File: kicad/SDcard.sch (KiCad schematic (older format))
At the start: 5 parts, among them J7 SD_Card, U25 74LVC244A

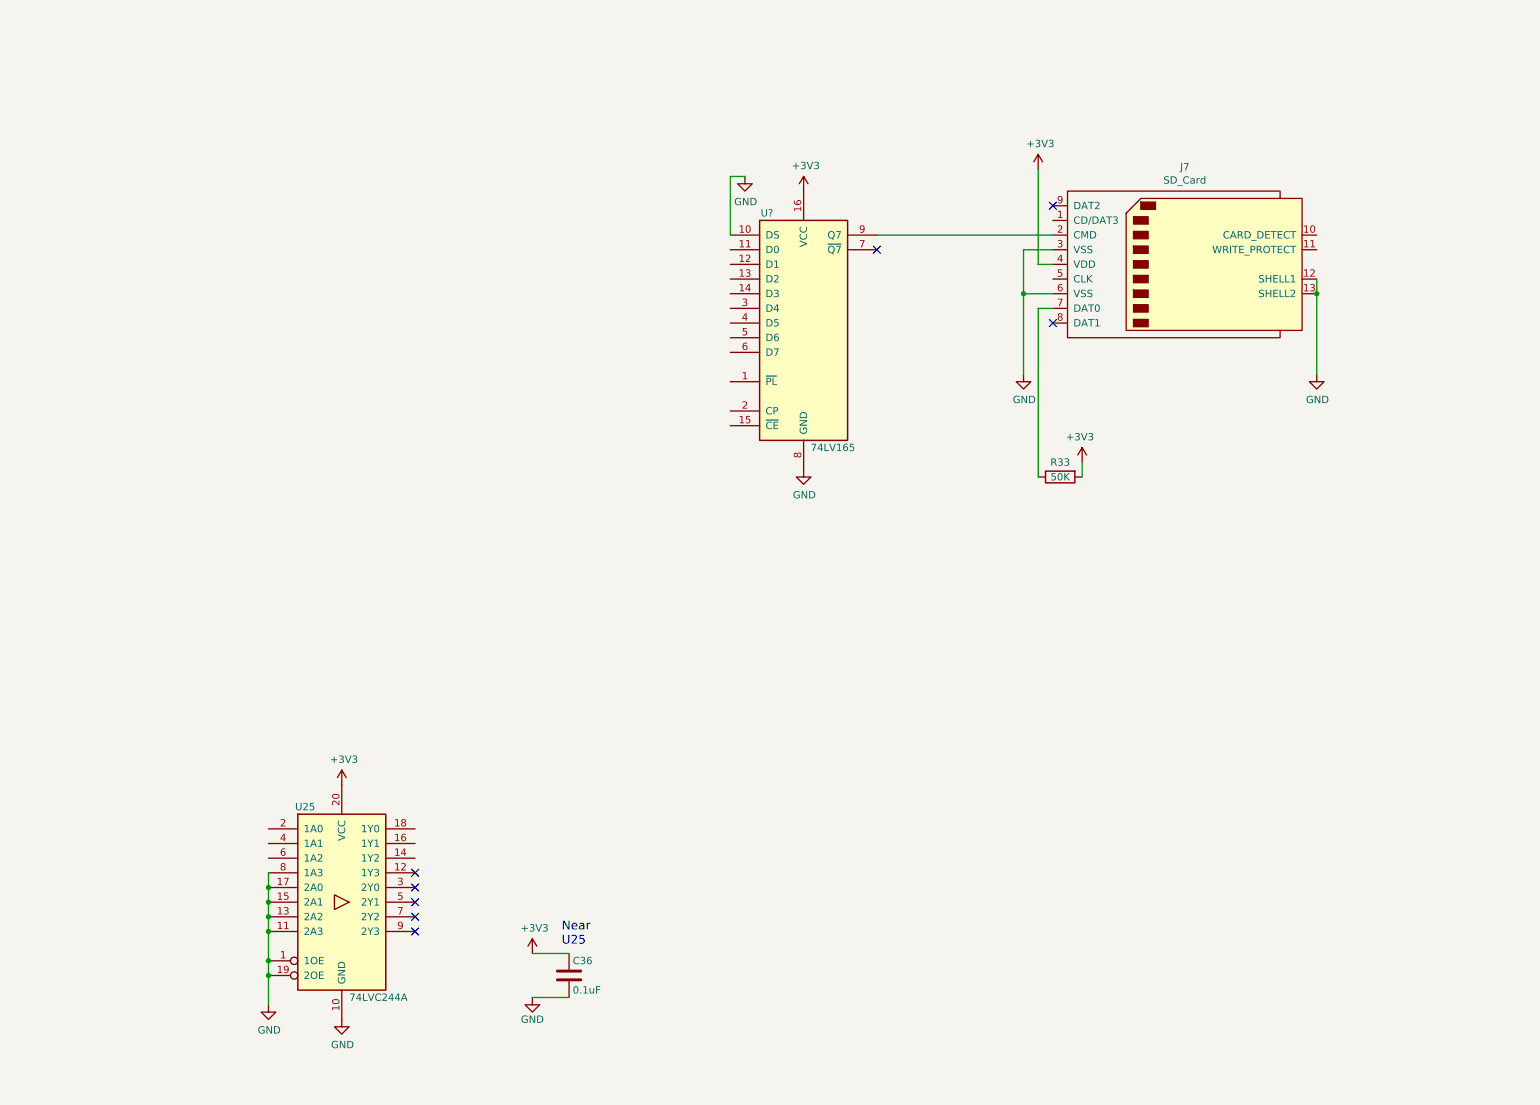
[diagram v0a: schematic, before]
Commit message: SDcard interface mostly complete.
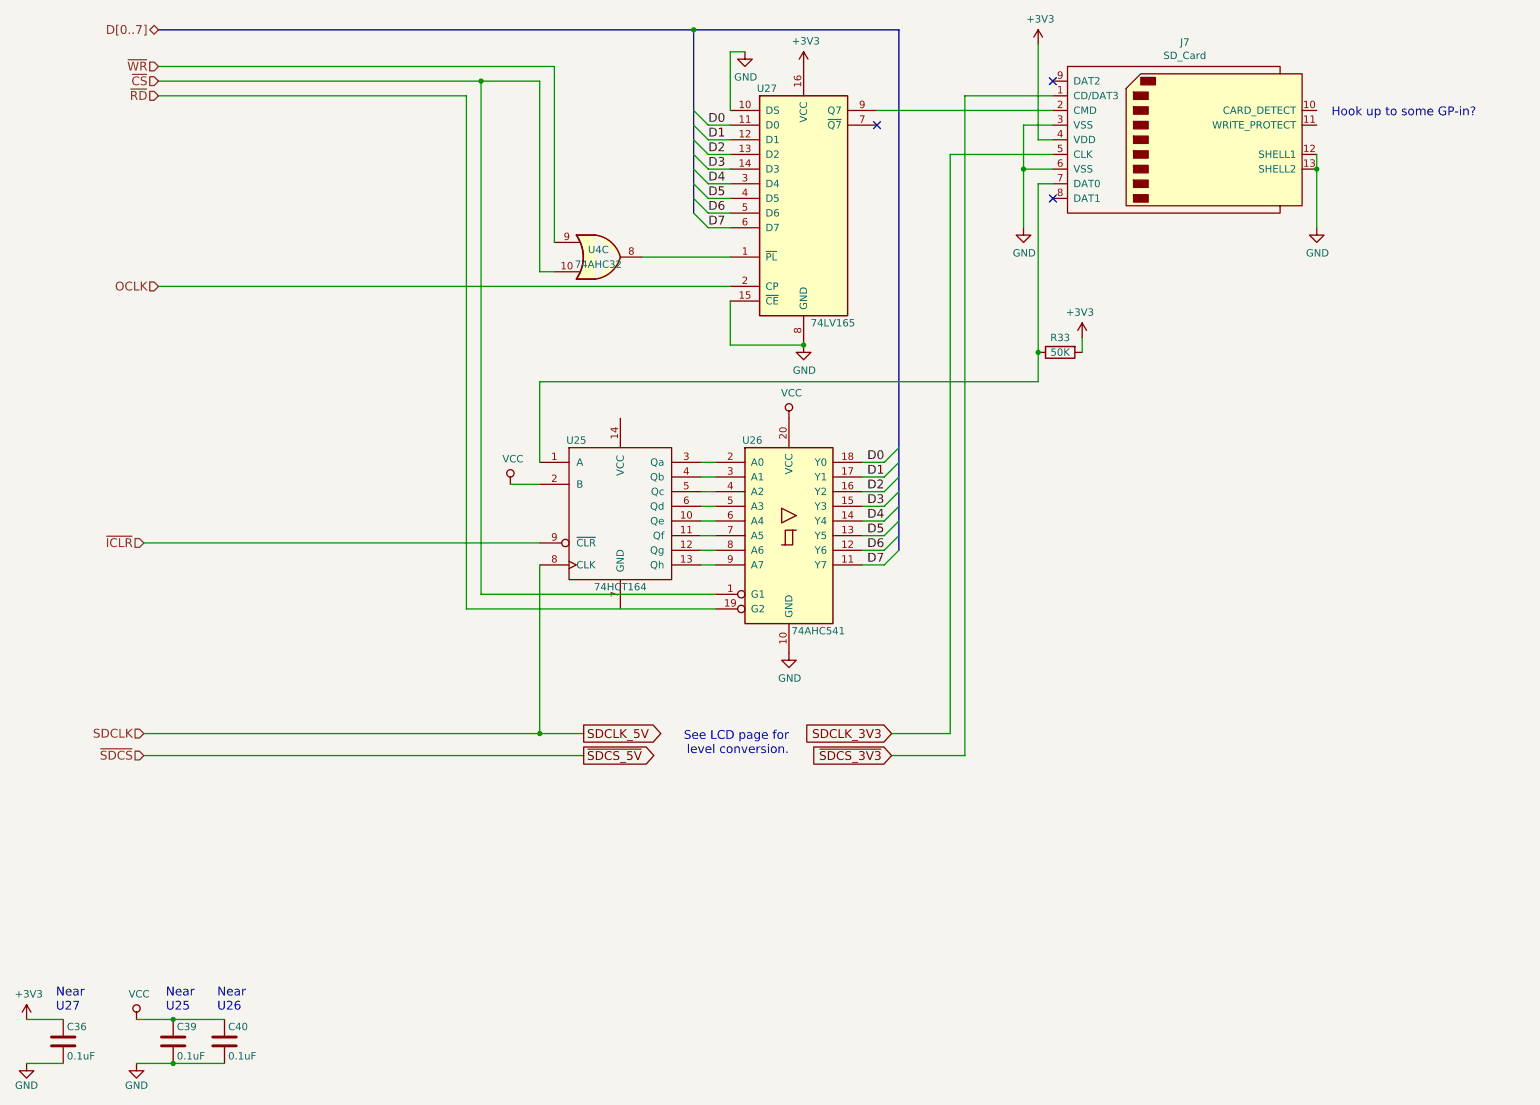
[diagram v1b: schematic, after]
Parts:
- removed U25: 74LVC244A, symbol 74xx:74HC244
- added C39, C40: 0.1uF, Capacitors_THT:C_Disc_D4.3mm_W1.9mm_P5.00mm, symbol Device:C
- added U25: 74HCT164, symbol headquarters:74HC164
- added U26: 74AHC541, symbol 74xx:74LS541
- added U4: 74AHC32, Housings_DIP:DIP-14_W7.62mm_LongPads, symbol 74xx:74LS32
- gave numbers to parts that had none: 1
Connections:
- net GND: now also U27.15 (~CE), C39.2, C40.2, U26.10 (GND)
- net at J7.7 (DAT0), R33.1: now also U25.1 (A)
- net at U27.1 (~PL): now also U4.8
- net D0: now reaches U27.11 (D0)
- net D0: now also U26.18 (Y0)
- net D1: now reaches U27.12 (D1)
- net D1: now also U26.17 (Y1)
- net D2: now reaches U27.13 (D2)
- net D2: now also U26.16 (Y2)
- net D3: now reaches U27.14 (D3)
- net D3: now also U26.15 (Y3)
- net OCLK: now reaches U27.2 (CP)
- net D4: now reaches U27.3 (D4)
- net D4: now also U26.14 (Y4)
- net D5: now reaches U27.4 (D5)
- net D5: now also U26.13 (Y5)
- net D6: now reaches U27.5 (D6)
- net D6: now also U26.12 (Y6)
- net D7: now reaches U27.6 (D7)
- net D7: now also U26.11 (Y7)
- net ~SDCS_3V3: now reaches J7.1 (CD/DAT3)
- net SDCLK_3V3: now reaches J7.5 (CLK)
- new net: U25.3 (Qa), U26.2 (A0)
- new net: U25.4 (Qb), U26.3 (A1)
- new net: U25.5 (Qc), U26.4 (A2)
- new net: U25.6 (Qd), U26.5 (A3)
- new net: U25.10 (Qe), U26.6 (A4)
- new net: U25.11 (Qf), U26.7 (A5)
- new net: U25.12 (Qg), U26.8 (A6)
- new net: U25.13 (Qh), U26.9 (A7)
- new net SDCLK_5V: U25.8 (CLK)
- new net VCC: C39.1, C40.1, U25.2 (B), U26.20 (VCC)
- new net ~CS: U26.1 (G1), U4.10
- new net ~ICLR: U25.9 (~CLR)
- new net ~RD: U26.19 (G2)
- new net ~WR: U4.9
- no-connect marks 8 -> 3
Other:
- note added: "Hook up to some GP-in?"
- note added: "Near\nU26"
- note added: "Near\nU27"
- note added: "See LCD page for\nlevel conversion."
- moved on the sheet: C36, J7, R33, U27

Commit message: Hook up SD card slot's write protect and card detect lines.
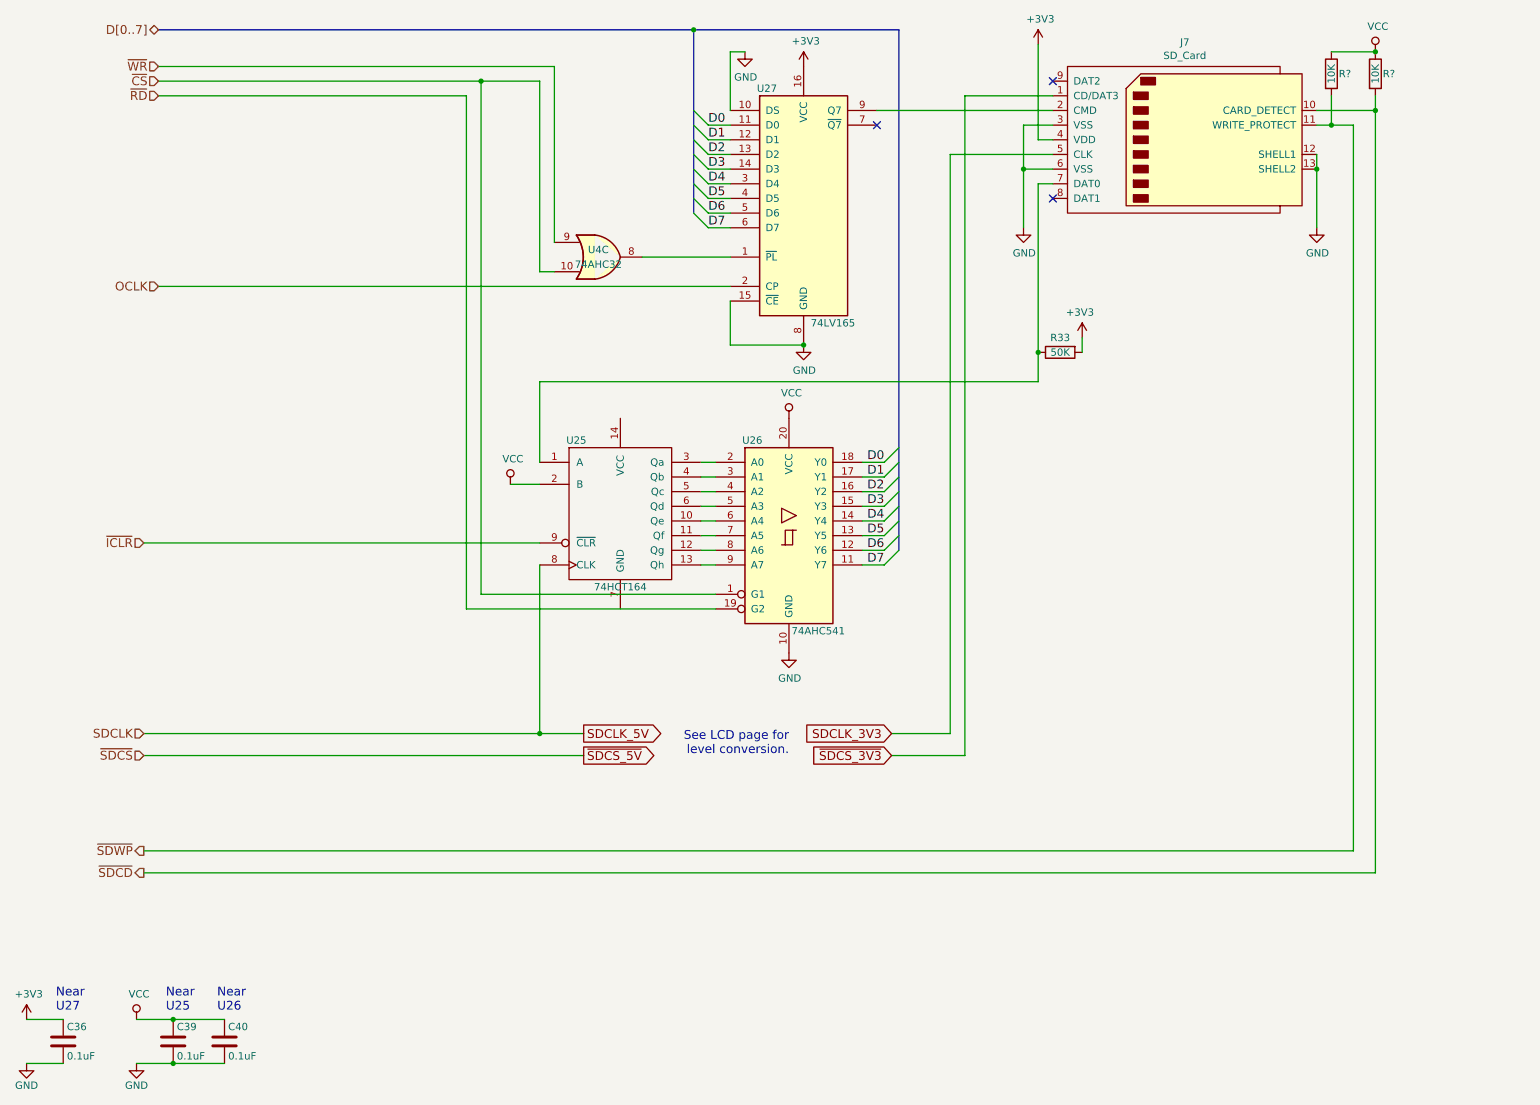
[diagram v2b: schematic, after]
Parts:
- added R? (x2): 10K, symbol Device:R
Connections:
- net VCC: now also R?.1, R?.1
- net ~SDCD: now reaches J7.10 (CARD_DETECT)
- net ~SDCD: now also R?.2
- net ~SDWP: now reaches J7.11 (WRITE_PROTECT)
- net ~SDWP: now also R?.2
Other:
- note removed: "Hook up to some GP-in?"
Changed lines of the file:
@@
 Wire Wire Line
 	3800 4550 5400 4550
-Text Notes 9600 1300 0    60   ~ 0
-Hook up to some GP-in?
 Text GLabel 6600 5500 0    60   Input ~ 0
 SDCLK_3V3
@@
 Wire Wire Line
 	2050 7750 1700 7750
+Connection ~ 1700 7750
+$Comp
+L Device:R R?
+U 1 1 5C96B667
+P 9900 1000
+F 0 "R?" H 9950 1000 50  0000 L CNN
+F 1 "10K" V 9900 1000 50  0000 C CNN
+F 2 "" V 9830 1000 50  0001 C CNN
+F 3 "~" H 9900 1000 50  0001 C CNN
+	1    9900 1000
+	1    0    0    -1
+$EndComp
+$Comp
+L Device:R R?
+U 1 1 5C96B6D4
+P 9600 1000
+F 0 "R?" H 9650 1000 50  0000 L CNN
+F 1 "10K" V 9600 1000 50  0000 C CNN
+F 2 "" V 9530 1000 50  0001 C CNN
+F 3 "~" H 9600 1000 50  0001 C CNN
+	1    9600 1000
+	1    0    0    -1
+$EndComp
+Wire Wire Line
+	9500 1350 9600 1350
+$Comp
+L power:VCC #PWR?
+U 1 1 5C96FF4A
+P 9900 850
+F 0 "#PWR?" H 9900 700 50  0001 C CNN
+F 1 "VCC" H 9917 1023 50  0000 C CNN
+F 2 "" H 9900 850 50  0001 C CNN
+F 3 "" H 9900 850 50  0001 C CNN
+	1    9900 850
+	1    0    0    -1
+$EndComp
+Wire Wire Line
+	9750 6300 1500 6300
+Wire Wire Line
+	9900 6450 1500 6450
+Text HLabel 1500 6300 0    60   Output ~ 0
+~SDWP
+Text HLabel 1500 6450 0    60   Output ~ 0
+~SDCD
+Wire Wire Line
+	9750 6300 9750 1350
+Wire Wire Line
+	9500 1250 9900 1250
+Wire Wire Line
+	9900 1150 9900 1250
+Connection ~ 9900 1250
+Wire Wire Line
+	9900 1250 9900 6450
+Wire Wire Line
+	9600 1150 9600 1350
+Connection ~ 9600 1350
+Wire Wire Line
+	9600 1350 9750 1350
 Wire Bus Line
 	5250 700  5250 1950
 Wire Bus Line
 	6650 700  6650 4250
-Connection ~ 1700 7750
+Wire Wire Line
+	9600 850  9900 850
+Connection ~ 9900 850
 $EndSCHEMATC

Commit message: Add audio output.
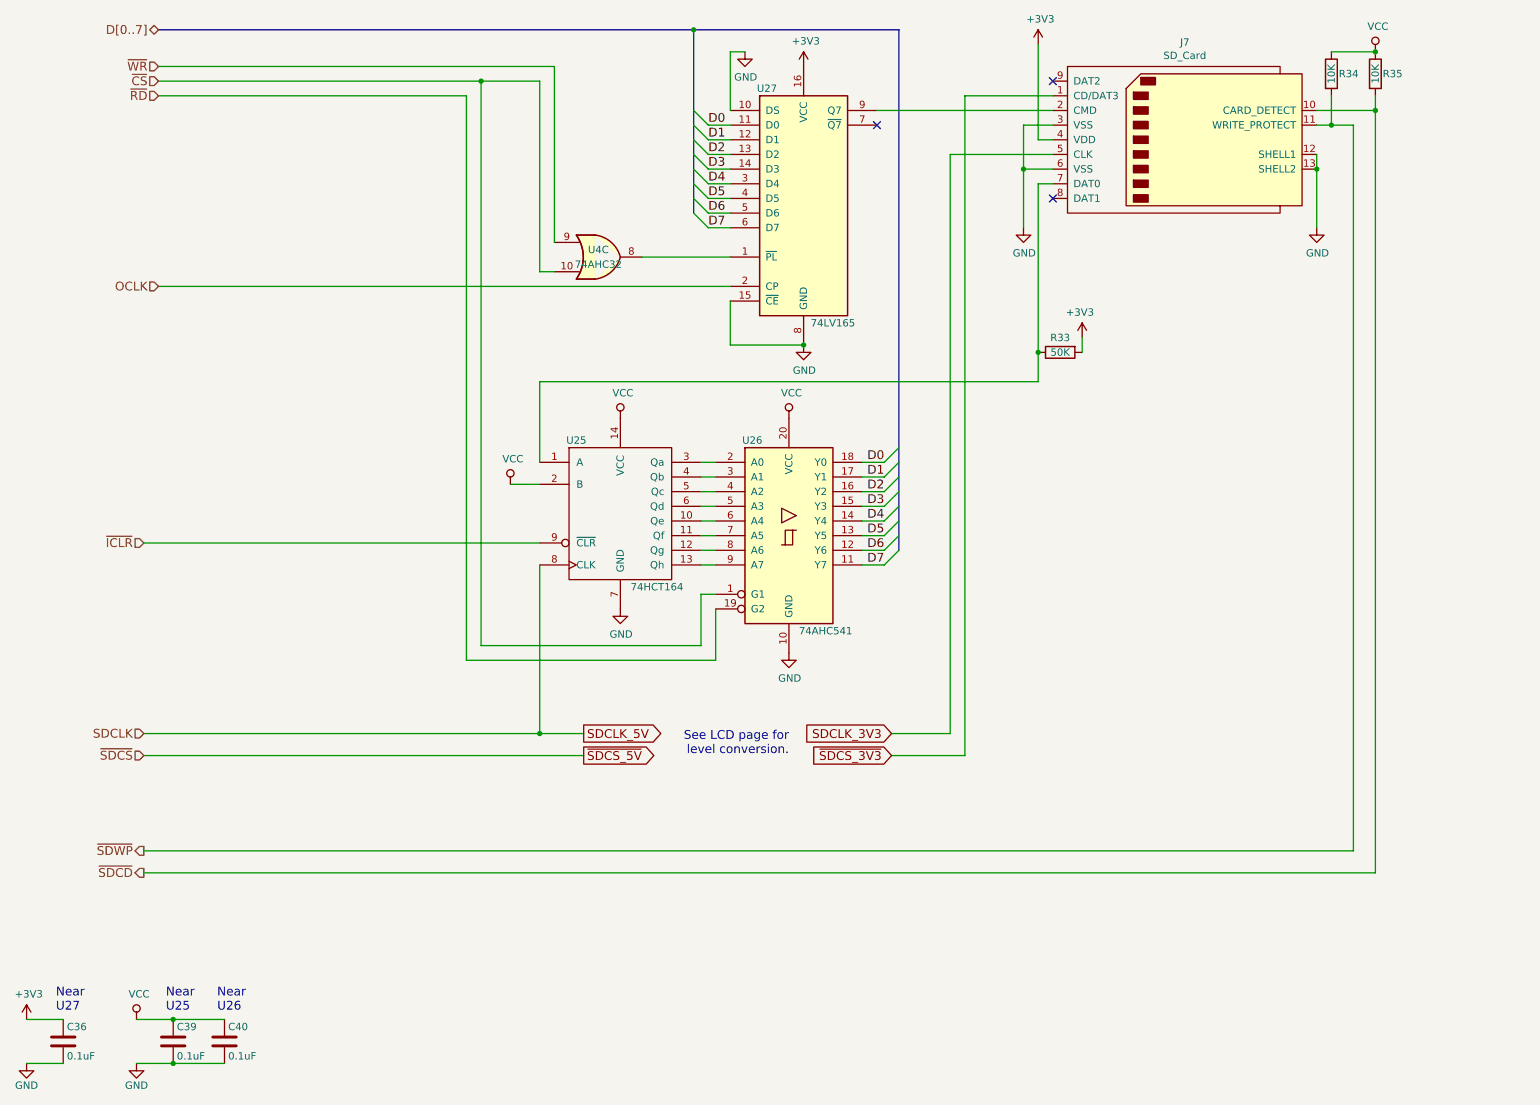
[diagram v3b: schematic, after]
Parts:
- gave numbers to parts that had none: 2
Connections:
- net GND: now also U25.7 (GND)
- net VCC: now also U25.14 (VCC)
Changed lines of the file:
@@
 EESchema Schematic File Version 4
 LIBS:z80-cache
-EELAYER 26 0
+EELAYER 29 0
 EELAYER END
 $Descr USLetter 11000 8500
 encoding utf-8
-Sheet 9 10
+Sheet 9 11
 Title "SD Card Interface"
 Date ""
@@
 P 5900 4150
 F 0 "U26" H 5650 4800 50  0000 C CNN
-F 1 "74AHC541" H 6100 3500 50  0000 C CNN
+F 1 "74AHC541" H 6150 3500 50  0000 C CNN
 F 2 "" H 5900 4150 50  0001 C CNN
 F 3 "http://www.ti.com/lit/gpn/sn74LS541" H 5900 4150 50  0001 C CNN
@@
 P 4750 4100
 F 0 "U25" H 4450 4700 50  0000 C CNN
-F 1 "74HCT164" H 4750 3700 50  0000 C CNN
+F 1 "74HCT164" H 5000 3700 50  0000 C CNN
 F 2 "" H 4600 4250 50  0001 C CNN
 F 3 "" H 4600 4250 50  0001 C CNN
@@
 Wire Wire Line
 	4200 5500 4500 5500
-Wire Wire Line
-	3800 4550 3800 1050
 Connection ~ 3800 1050
 Wire Wire Line
 	3800 1050 4200 1050
 Wire Wire Line
-	3700 1150 3700 4650
-Wire Wire Line
-	3700 4650 5400 4650
-Wire Wire Line
 	1600 1150 3700 1150
-Wire Wire Line
-	3800 4550 5400 4550
 Text GLabel 6600 5500 0    60   Input ~ 0
 SDCLK_3V3
@@
 Connection ~ 1700 7750
 $Comp
-L Device:R R?
+L Device:R R35
 U 1 1 5C96B667
 P 9900 1000
-F 0 "R?" H 9950 1000 50  0000 L CNN
+F 0 "R35" H 9950 1000 50  0000 L CNN
 F 1 "10K" V 9900 1000 50  0000 C CNN
 F 2 "" V 9830 1000 50  0001 C CNN
@@
 $EndComp
 $Comp
-L Device:R R?
+L Device:R R34
 U 1 1 5C96B6D4
 P 9600 1000
-F 0 "R?" H 9650 1000 50  0000 L CNN
+F 0 "R34" H 9650 1000 50  0000 L CNN
 F 1 "10K" V 9600 1000 50  0000 C CNN
 F 2 "" V 9530 1000 50  0001 C CNN
@@
 	9500 1350 9600 1350
 $Comp
-L power:VCC #PWR?
+L power:VCC #PWR0121
 U 1 1 5C96FF4A
 P 9900 850
-F 0 "#PWR?" H 9900 700 50  0001 C CNN
+F 0 "#PWR0121" H 9900 700 50  0001 C CNN
 F 1 "VCC" H 9917 1023 50  0000 C CNN
 F 2 "" H 9900 850 50  0001 C CNN
@@
 Wire Wire Line
 	9600 1350 9750 1350
+Wire Wire Line
+	9600 850  9900 850
+Connection ~ 9900 850
+$Comp
+L power:VCC #PWR0142
+U 1 1 5CC2D81F
+P 4750 3350
+F 0 "#PWR0142" H 4750 3200 50  0001 C CNN
+F 1 "VCC" H 4767 3523 50  0000 C CNN
+F 2 "" H 4750 3350 50  0001 C CNN
+F 3 "" H 4750 3350 50  0001 C CNN
+	1    4750 3350
+	1    0    0    -1
+$EndComp
+$Comp
+L power:GND #PWR0143
+U 1 1 5CC2EAFB
+P 4750 4650
+F 0 "#PWR0143" H 4750 4400 50  0001 C CNN
+F 1 "GND" H 4755 4477 50  0000 C CNN
+F 2 "" H 4750 4650 50  0001 C CNN
+F 3 "" H 4750 4650 50  0001 C CNN
+	1    4750 4650
+	1    0    0    -1
+$EndComp
+Wire Wire Line
+	5400 4650 5400 5000
+Wire Wire Line
+	5400 5000 3700 5000
+Wire Wire Line
+	3700 1150 3700 5000
+Wire Wire Line
+	3800 4900 5300 4900
+Wire Wire Line
+	5300 4900 5300 4550
+Wire Wire Line
+	5300 4550 5400 4550
+Wire Wire Line
+	3800 1050 3800 4900
 Wire Bus Line
 	5250 700  5250 1950
 Wire Bus Line
 	6650 700  6650 4250
-Wire Wire Line
-	9600 850  9900 850
-Connection ~ 9900 850
 $EndSCHEMATC

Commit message: Assign footprints.
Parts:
- R33, R34, R35: footprint (none) -> Resistors_SMD:R_0805_HandSoldering
- U25: footprint (none) -> Housings_SSOP:TSSOP-14_4.4x5mm_Pitch0.65mm
- U26: footprint (none) -> Housings_SSOP:TSSOP-20_4.4x6.5mm_Pitch0.65mm
- U27: footprint (none) -> Housings_SSOP:TSSOP-16_4.4x5mm_Pitch0.65mm
- U4: footprint Housings_DIP:DIP-14_W7.62mm_LongPads -> Housings_DIP:DIP-14_W7.62mm
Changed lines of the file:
@@
 F 0 "R33" V 7650 2900 50  0000 C CNN
 F 1 "50K" V 7750 2900 50  0000 C CNN
-F 2 "" V 7680 2900 50  0001 C CNN
+F 2 "Resistors_SMD:R_0805_HandSoldering" V 7680 2900 50  0001 C CNN
 F 3 "~" H 7750 2900 50  0001 C CNN
 	1    7750 2900
@@
 F 0 "U27" H 5750 2600 50  0000 C CNN
 F 1 "74LV165" H 6200 1000 50  0000 C CNN
-F 2 "" H 6000 1850 50  0001 C CNN
+F 2 "Housings_SSOP:TSSOP-16_4.4x5mm_Pitch0.65mm" H 6000 1850 50  0001 C CNN
 F 3 "http://www.ti.com/lit/gpn/sn74LS165" H 6000 1850 50  0001 C CNN
 	1    6000 1850
@@
 F 0 "U4" H 4600 2300 50  0000 C CNN
 F 1 "74AHC32" H 4600 2200 50  0000 C CNN
-F 2 "Housings_DIP:DIP-14_W7.62mm_LongPads" H 4600 2250 50  0001 C CNN
+F 2 "Housings_DIP:DIP-14_W7.62mm" H 4600 2250 50  0001 C CNN
 F 3 "" H 4600 2250 50  0001 C CNN
 	3    4600 2250
@@
 F 0 "U26" H 5650 4800 50  0000 C CNN
 F 1 "74AHC541" H 6150 3500 50  0000 C CNN
-F 2 "" H 5900 4150 50  0001 C CNN
+F 2 "Housings_SSOP:TSSOP-20_4.4x6.5mm_Pitch0.65mm" H 5900 4150 50  0001 C CNN
 F 3 "http://www.ti.com/lit/gpn/sn74LS541" H 5900 4150 50  0001 C CNN
 	1    5900 4150
@@
 F 0 "U25" H 4450 4700 50  0000 C CNN
 F 1 "74HCT164" H 5000 3700 50  0000 C CNN
-F 2 "" H 4600 4250 50  0001 C CNN
+F 2 "Housings_SSOP:TSSOP-14_4.4x5mm_Pitch0.65mm" H 4600 4250 50  0001 C CNN
 F 3 "" H 4600 4250 50  0001 C CNN
 	1    4750 4100
@@
 F 0 "R35" H 9950 1000 50  0000 L CNN
 F 1 "10K" V 9900 1000 50  0000 C CNN
-F 2 "" V 9830 1000 50  0001 C CNN
+F 2 "Resistors_SMD:R_0805_HandSoldering" V 9830 1000 50  0001 C CNN
 F 3 "~" H 9900 1000 50  0001 C CNN
 	1    9900 1000
@@
 F 0 "R34" H 9650 1000 50  0000 L CNN
 F 1 "10K" V 9600 1000 50  0000 C CNN
-F 2 "" V 9530 1000 50  0001 C CNN
+F 2 "Resistors_SMD:R_0805_HandSoldering" V 9530 1000 50  0001 C CNN
 F 3 "~" H 9600 1000 50  0001 C CNN
 	1    9600 1000
